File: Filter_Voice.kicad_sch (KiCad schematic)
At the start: 25 parts, among them U1 TL074, U4 SSI2140

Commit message: Controls PCB lay out
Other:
- moved on the sheet: C14, R31, R32, R38
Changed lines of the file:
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@@
   (junction (at 46.99 67.31) (diameter 0) (color 0 0 0 0)
   )
-  (junction (at 201.93 55.88) (diameter 0) (color 0 0 0 0)
+  (junction (at 201.93 53.34) (diameter 0) (color 0 0 0 0)
   )
   (junction (at 111.76 50.8) (diameter 0) (color 0 0 0 0)
   )
-  (junction (at 222.25 62.23) (diameter 0) (color 0 0 0 0)
-  )
   (junction (at 67.31 72.39) (diameter 0) (color 0 0 0 0)
   )
@@
   (junction (at 60.96 102.87) (diameter 0) (color 0 0 0 0)
   )
+  (junction (at 222.25 60.96) (diameter 0) (color 0 0 0 0)
+  )
   (junction (at 60.96 97.79) (diameter 0) (color 0 0 0 0)
   )
@@
   (junction (at 90.17 111.76) (diameter 0) (color 0 0 0 0)
   )
-  (junction (at 201.93 62.23) (diameter 0) (color 0 0 0 0)
+  (junction (at 201.93 60.96) (diameter 0) (color 0 0 0 0)
   )
   (junction (at 67.31 87.63) (diameter 0) (color 0 0 0 0)
@@
     (stroke (width 0) (type default))
   )
+  (wire (pts (xy 201.93 53.34) (xy 201.93 60.96))
+    (stroke (width 0) (type default))
+  )
   (wire (pts (xy 67.31 87.63) (xy 77.47 87.63))
     (stroke (width 0) (type default))
@@
     (stroke (width 0) (type default))
   )
-  (wire (pts (xy 222.25 55.88) (xy 222.25 62.23))
+  (wire (pts (xy 222.25 53.34) (xy 222.25 60.96))
     (stroke (width 0) (type default))
   )
@@
     (stroke (width 0) (type default))
   )
-  (wire (pts (xy 201.93 68.58) (xy 201.93 62.23))
-    (stroke (width 0) (type default))
-  )
-  (wire (pts (xy 196.85 62.23) (xy 201.93 62.23))
+  (wire (pts (xy 201.93 60.96) (xy 201.93 68.58))
+    (stroke (width 0) (type default))
+  )
+  (wire (pts (xy 196.85 60.96) (xy 201.93 60.96))
     (stroke (width 0) (type default))
   )
@@
     (stroke (width 0) (type default))
   )
-  (wire (pts (xy 201.93 55.88) (xy 209.55 55.88))
+  (wire (pts (xy 201.93 53.34) (xy 209.55 53.34))
     (stroke (width 0) (type default))
   )
@@
     (stroke (width 0) (type default))
   )
-  (wire (pts (xy 214.63 55.88) (xy 222.25 55.88))
+  (wire (pts (xy 214.63 53.34) (xy 222.25 53.34))
     (stroke (width 0) (type default))
   )
@@
     (stroke (width 0) (type default))
   )
-  (wire (pts (xy 222.25 62.23) (xy 222.25 71.12))
-    (stroke (width 0) (type default))
-  )
-  (wire (pts (xy 201.93 55.88) (xy 201.93 62.23))
+  (wire (pts (xy 222.25 60.96) (xy 222.25 71.12))
     (stroke (width 0) (type default))
   )
@@
     (stroke (width 0) (type default))
   )
-  (wire (pts (xy 196.85 55.88) (xy 201.93 55.88))
+  (wire (pts (xy 196.85 53.34) (xy 201.93 53.34))
     (stroke (width 0) (type default))
   )
@@
     (stroke (width 0) (type default))
   )
-  (wire (pts (xy 201.93 62.23) (xy 209.55 62.23))
+  (wire (pts (xy 201.93 60.96) (xy 209.55 60.96))
     (stroke (width 0) (type default))
   )
@@
     (stroke (width 0) (type default))
   )
-  (wire (pts (xy 189.23 62.23) (xy 191.77 62.23))
+  (wire (pts (xy 189.23 60.96) (xy 191.77 60.96))
     (stroke (width 0) (type default))
   )
@@
     (stroke (width 0) (type default))
   )
-  (wire (pts (xy 189.23 55.88) (xy 191.77 55.88))
+  (wire (pts (xy 189.23 53.34) (xy 191.77 53.34))
     (stroke (width 0) (type default))
   )
@@
     (stroke (width 0) (type default))
   )
-  (wire (pts (xy 214.63 62.23) (xy 222.25 62.23))
+  (wire (pts (xy 214.63 60.96) (xy 222.25 60.96))
     (stroke (width 0) (type default))
   )
@@
     (effects (font (size 1.27 1.27)) (justify left bottom))
   )
-  (hierarchical_label "FREQ_CV1" (shape input) (at 189.23 55.88 180) (fields_autoplaced)
+  (hierarchical_label "FREQ_CV1" (shape input) (at 189.23 53.34 180) (fields_autoplaced)
     (effects (font (size 1.27 1.27)) (justify right))
   )
@@
     (effects (font (size 1.27 1.27)) (justify left))
   )
-  (hierarchical_label "FREQ_CV2" (shape input) (at 189.23 62.23 180) (fields_autoplaced)
+  (hierarchical_label "FREQ_CV2" (shape input) (at 189.23 60.96 180) (fields_autoplaced)
     (effects (font (size 1.27 1.27)) (justify right))
   )
-  (symbol (lib_id "Device:R_Small") (at 194.31 55.88 270) (unit 1)
-    (in_bom yes) (on_board yes) (dnp no)
-    (property "Reference" "R31" (at 194.31 58.42 90)
-      (effects (font (size 1.27 1.27)))
-    )
-    (property "Value" "100k" (at 194.31 53.34 90)
-      (effects (font (size 1.27 1.27)))
-    )
-    (property "Footprint" "Resistor_SMD:R_0603_1608Metric_Pad0.98x0.95mm_HandSolder" (at 194.31 55.88 0)
-      (effects (font (size 1.27 1.27)) hide)
-    )
-    (property "Datasheet" "~" (at 194.31 55.88 0)
+  (symbol (lib_id "Device:R_Small") (at 194.31 53.34 270) (unit 1)
+    (in_bom yes) (on_board yes) (dnp no)
+    (property "Reference" "R31" (at 194.31 55.88 90)
+      (effects (font (size 1.27 1.27)))
+    )
+    (property "Value" "100k" (at 194.31 50.8 90)
+      (effects (font (size 1.27 1.27)))
+    )
+    (property "Footprint" "Resistor_SMD:R_0603_1608Metric_Pad0.98x0.95mm_HandSolder" (at 194.31 53.34 0)
+      (effects (font (size 1.27 1.27)) hide)
+    )
+    (property "Datasheet" "~" (at 194.31 53.34 0)
       (effects (font (size 1.27 1.27)) hide)
     )
@@
     )
   )
-  (symbol (lib_id "Device:R_Small") (at 194.31 62.23 270) (unit 1)
-    (in_bom yes) (on_board yes) (dnp no)
-    (property "Reference" "R32" (at 194.31 64.77 90)
-      (effects (font (size 1.27 1.27)))
-    )
-    (property "Value" "100k" (at 194.31 59.69 90)
-      (effects (font (size 1.27 1.27)))
-    )
-    (property "Footprint" "Resistor_SMD:R_0603_1608Metric_Pad0.98x0.95mm_HandSolder" (at 194.31 62.23 0)
-      (effects (font (size 1.27 1.27)) hide)
-    )
-    (property "Datasheet" "~" (at 194.31 62.23 0)
+  (symbol (lib_id "Device:R_Small") (at 194.31 60.96 270) (unit 1)
+    (in_bom yes) (on_board yes) (dnp no)
+    (property "Reference" "R32" (at 194.31 63.5 90)
+      (effects (font (size 1.27 1.27)))
+    )
+    (property "Value" "100k" (at 194.31 58.42 90)
+      (effects (font (size 1.27 1.27)))
+    )
+    (property "Footprint" "Resistor_SMD:R_0603_1608Metric_Pad0.98x0.95mm_HandSolder" (at 194.31 60.96 0)
+      (effects (font (size 1.27 1.27)) hide)
+    )
+    (property "Datasheet" "~" (at 194.31 60.96 0)
       (effects (font (size 1.27 1.27)) hide)
     )
@@
     )
   )
-  (symbol (lib_id "Device:R_Small") (at 212.09 62.23 270) (unit 1)
-    (in_bom yes) (on_board yes) (dnp no)
-    (property "Reference" "R38" (at 212.09 64.77 90)
-      (effects (font (size 1.27 1.27)))
-    )
-    (property "Value" "150k" (at 212.09 59.69 90)
-      (effects (font (size 1.27 1.27)))
-    )
-    (property "Footprint" "Resistor_SMD:R_0603_1608Metric_Pad0.98x0.95mm_HandSolder" (at 212.09 62.23 0)
-      (effects (font (size 1.27 1.27)) hide)
-    )
-    (property "Datasheet" "~" (at 212.09 62.23 0)
+  (symbol (lib_id "Device:R_Small") (at 212.09 60.96 270) (unit 1)
+    (in_bom yes) (on_board yes) (dnp no)
+    (property "Reference" "R38" (at 212.09 63.5 90)
+      (effects (font (size 1.27 1.27)))
+    )
+    (property "Value" "150k" (at 212.09 58.42 90)
+      (effects (font (size 1.27 1.27)))
+    )
+    (property "Footprint" "Resistor_SMD:R_0603_1608Metric_Pad0.98x0.95mm_HandSolder" (at 212.09 60.96 0)
+      (effects (font (size 1.27 1.27)) hide)
+    )
+    (property "Datasheet" "~" (at 212.09 60.96 0)
       (effects (font (size 1.27 1.27)) hide)
     )
@@
     )
   )
-  (symbol (lib_id "Device:C_Small") (at 212.09 55.88 90) (unit 1)
-    (in_bom yes) (on_board yes) (dnp no)
-    (property "Reference" "C14" (at 214.63 52.07 90)
-      (effects (font (size 1.27 1.27)))
-    )
-    (property "Value" "10nF" (at 209.55 52.07 90)
-      (effects (font (size 1.27 1.27)))
-    )
-    (property "Footprint" "Capacitor_SMD:C_0603_1608Metric_Pad1.08x0.95mm_HandSolder" (at 212.09 55.88 0)
-      (effects (font (size 1.27 1.27)) hide)
-    )
-    (property "Datasheet" "~" (at 212.09 55.88 0)
-      (effects (font (size 1.27 1.27)) hide)
-    )
+  (symbol (lib_id "Device:C_Small") (at 212.09 53.34 90) (unit 1)
+    (in_bom yes) (on_board yes) (dnp no)
+    (property "Reference" "C14" (at 214.63 49.53 90)
+      (effects (font (size 1.27 1.27)))
+    )
+    (property "Value" "10nF" (at 209.55 49.53 90)
+      (effects (font (size 1.27 1.27)))
+    )
+    (property "Footprint" "Capacitor_SMD:C_0603_1608Metric_Pad1.08x0.95mm_HandSolder" (at 212.09 53.34 0)
+      (effects (font (size 1.27 1.27)) hide)
+    )
+    (property "Datasheet" "~" (at 212.09 53.34 0)
+      (effects (font (size 1.27 1.27)) hide)
+    )

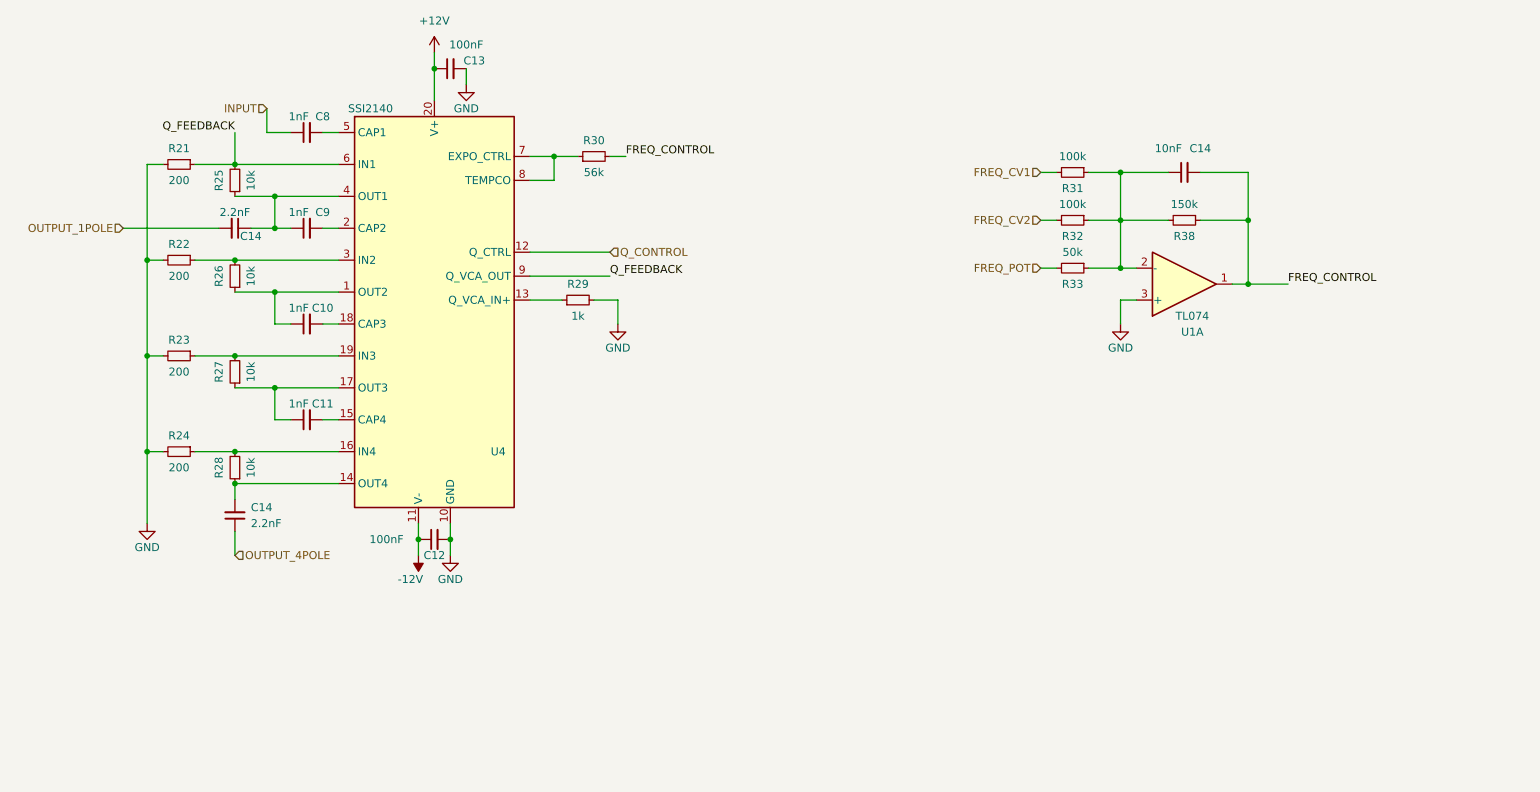
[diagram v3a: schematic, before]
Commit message: Started generating JLC placement details
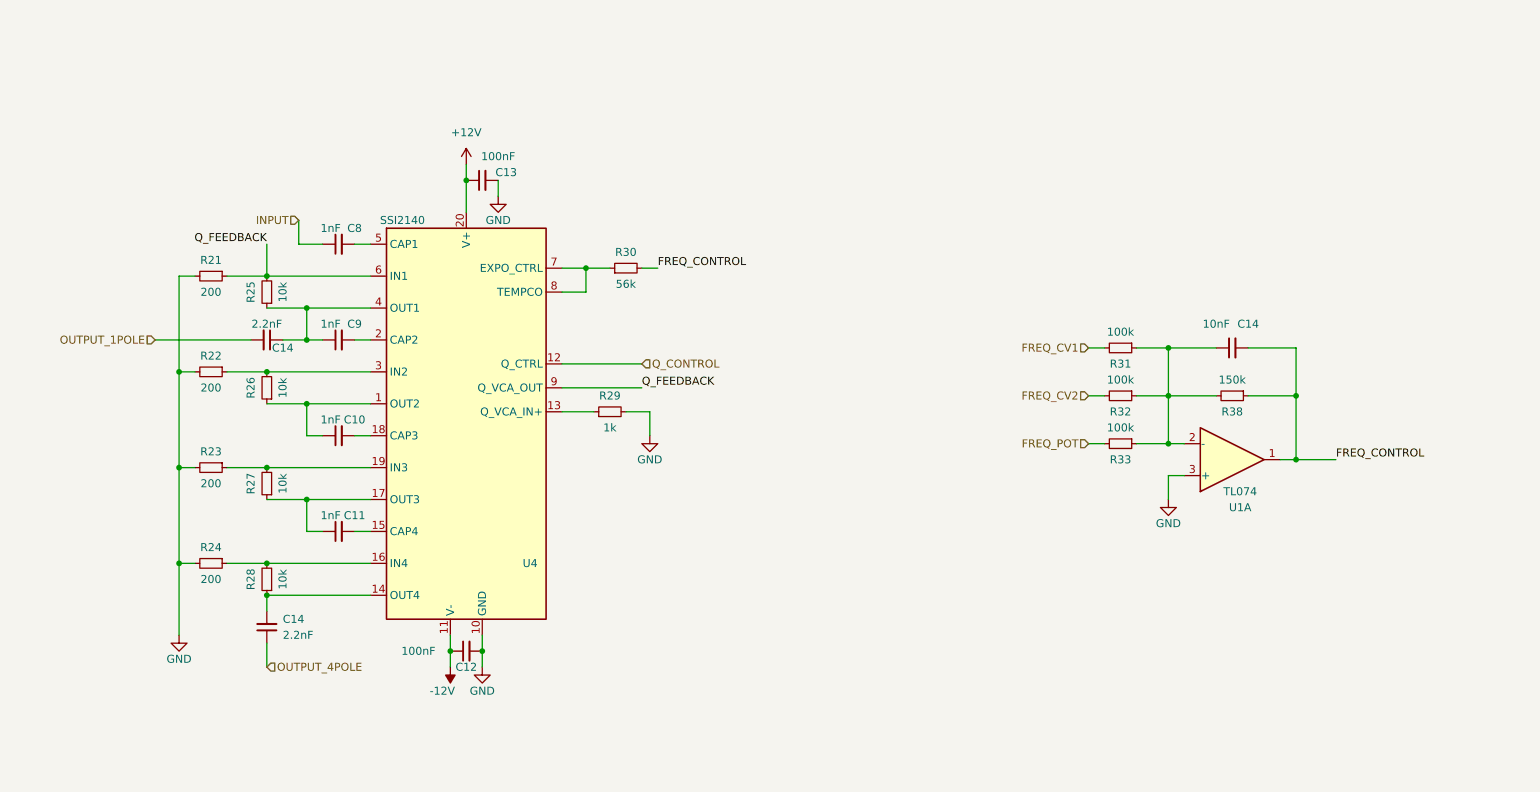
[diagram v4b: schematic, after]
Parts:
- R33: value 50k -> 100k
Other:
- moved on the sheet: C10, C11, C12, C13, C14, C8, C9, R21, R22, R23, R24, R25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

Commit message: Updated SSI2149 symbol; cleaned up routing on component board
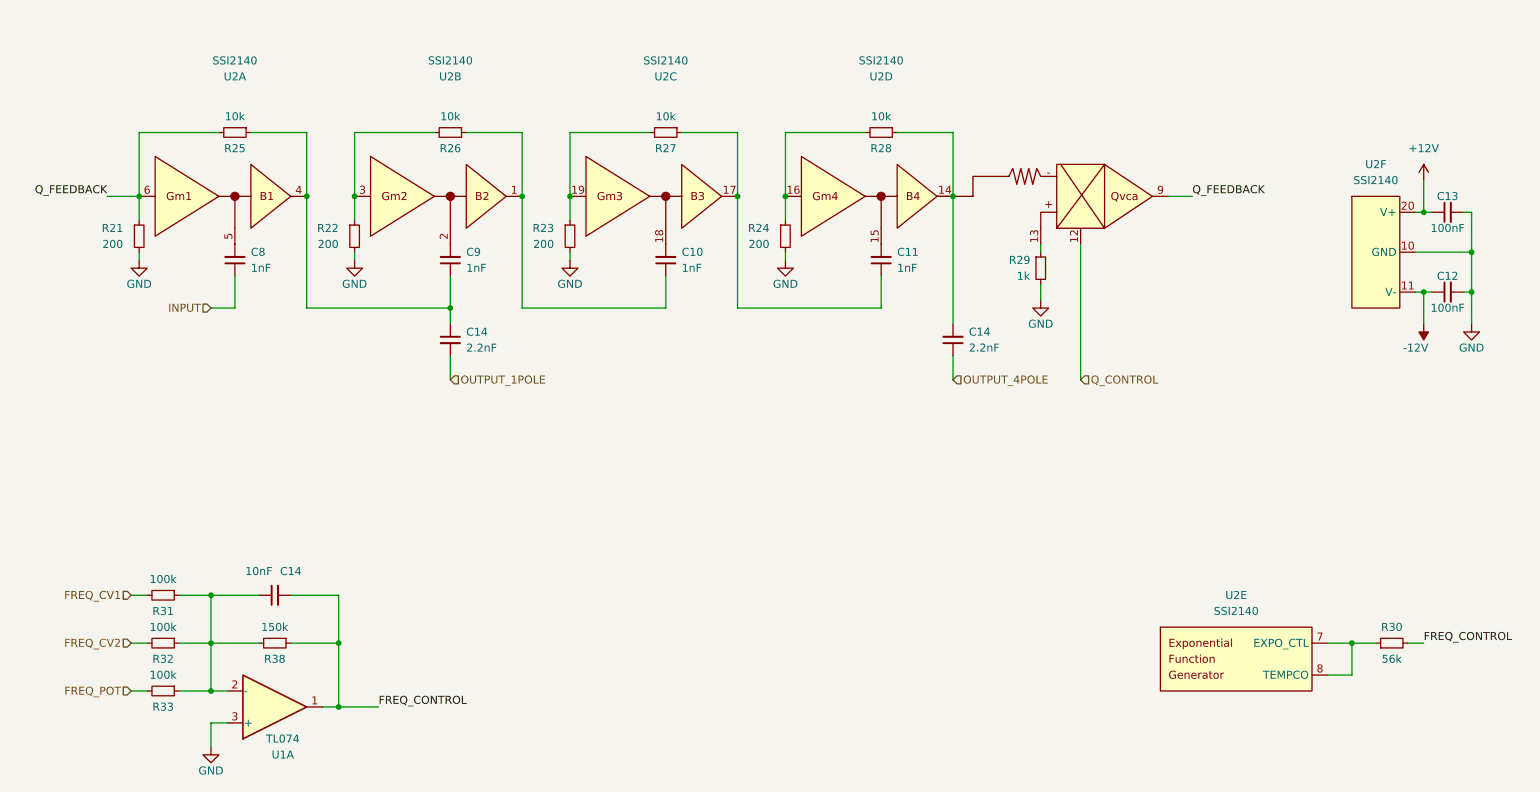
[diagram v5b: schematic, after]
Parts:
- removed U4: SSI2140, Package_SO:SSOP-20_4.4x6.5mm_P0.65mm, symbol Mountjoy:SSI2140
- added U2: SSI2140, Package_SO:TSSOP-20_4.4x6.5mm_P0.65mm, symbol SSI2140:SSI2140
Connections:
- net +12V: now also U2.20 (V+)
- net -12V: now also U2.11 (V-)
- net GND: now also U2.10 (GND)
- net Q_CONTROL: now also U2.12
- net Q_FEEDBACK: now also U2.6, U2.9
- net at C10.1, R26.1: now also U2.1
- net at C10.2: now also U2.18
- net at C14.2, R28.1: now also U2.14
- net at R29.1: now also U2.13
- net at C11.2: now also U2.15
- net at R24.1, R28.2: now also U2.16
- net at C11.1, R27.1: now also U2.17
- net at R23.1, R27.2: now also U2.19
- net at C9.2: now also U2.2
- net at R22.1, R26.2: now also U2.3
- net at C14.1, C9.1, R25.1: now also U2.4
- net at C8.2: now also U2.5
- net at R30.1: now also U2.7 (EXPO_CTL), U2.8 (TEMPCO)
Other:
- moved on the sheet: C10, C11, C12, C13, C14, C8, C9, R21, R22, R23, R24, R25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

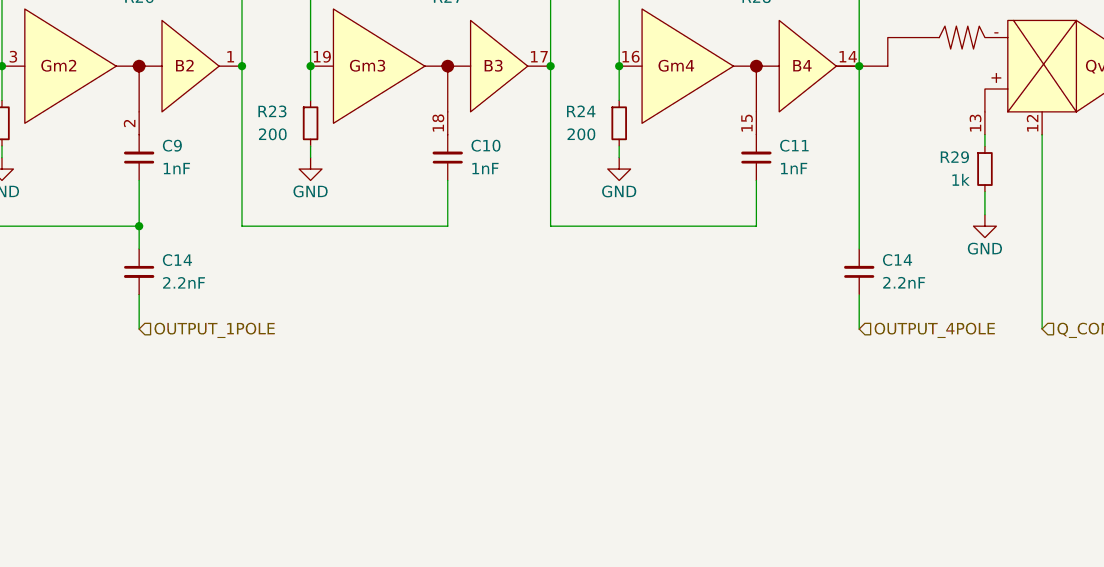
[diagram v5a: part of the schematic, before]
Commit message: Added v1.0 component schematic pdf
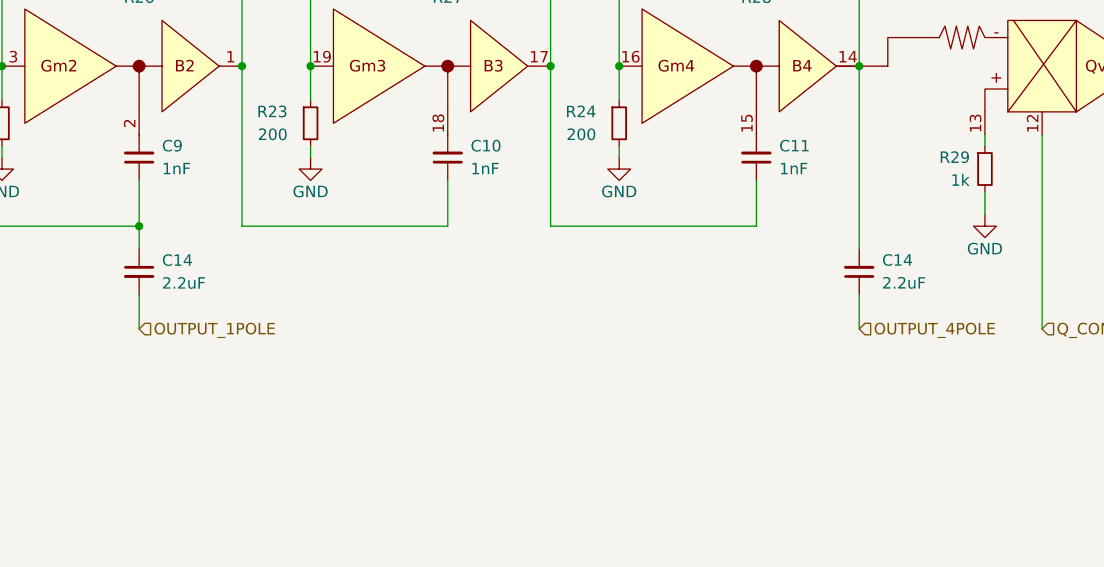
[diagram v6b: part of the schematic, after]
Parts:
- C14: value 2.2nF -> 2.2uF
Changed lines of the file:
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@@
       (effects (font (size 1.27 1.27)) (justify right))
     )
-    (property "Value" "2.2nF" (at 177.8 81.2736 0)
+    (property "Value" "2.2uF" (at 177.8 81.2736 0)
       (effects (font (size 1.27 1.27)) (justify right))
     )
@@
       (effects (font (size 1.27 1.27)) (justify left))
     )
-    (property "Value" "2.2nF" (at 97.79 81.2863 0)
+    (property "Value" "2.2uF" (at 97.79 81.2863 0)
       (effects (font (size 1.27 1.27)) (justify left))
     )

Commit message: Minor changes
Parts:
- added R72: 10k, Resistor_SMD:R_0603_1608Metric_Pad0.98x0.95mm_HandSolder, symbol Device:R_Small
- added R73: 14k, Resistor_SMD:R_0603_1608Metric_Pad0.98x0.95mm_HandSolder, symbol Device:R_Small
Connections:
- net GND: now also R73.2
- net INPUT: now also R72.1; no longer C8.1
- new net Audio_in_Scaled: C8.1, R72.2, R73.1
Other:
- note added: "Input scaling - filters can only process +5v to -5v without clipping 10k/14k scales input by x0.583"
- company: (none) -> Mountjoy Modular
- title: (none) -> Hypersoniq
- moved on the sheet: C14, R31, R32, R33, R38, U1A
